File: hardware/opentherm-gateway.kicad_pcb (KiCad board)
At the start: 4 copper layers, 56 x 42 mm, 83 parts, among them J1 BOILER, J2 THERM, J3 USB-C, J5 5V IN, J6 NTC, Q1 MMBT2907A, Q2 MMBT2907A, Q3 MMBT2907A, Q4 MMBT2907A, Q5 MMBT2222A, Q6 MMBT2222A, SW1 RESET, SW2 BOOT, U1 MT3540-F23, U2 LTV-817S, U3 LTV-817S, U4 ESP32-C3-WROOM-02-N4, U5 AP2112K-3.3, U6 USBLC6-2SC6

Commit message: hardware: complete BOM with LCSC part numbers (JLCPCB format too), fix ESP32 module code, R17 330R for the green LED
Co-Authored-By: Claude Sonnet 5.5 <noreply@anthropic.com>
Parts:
- R17: value 1k -> 330
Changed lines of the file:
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@@
 			)
 		)
-		(property "Value" "1k"
+		(property "Value" "330"
 			(at 0 -1.65 180)
 			(layer "B.Fab")

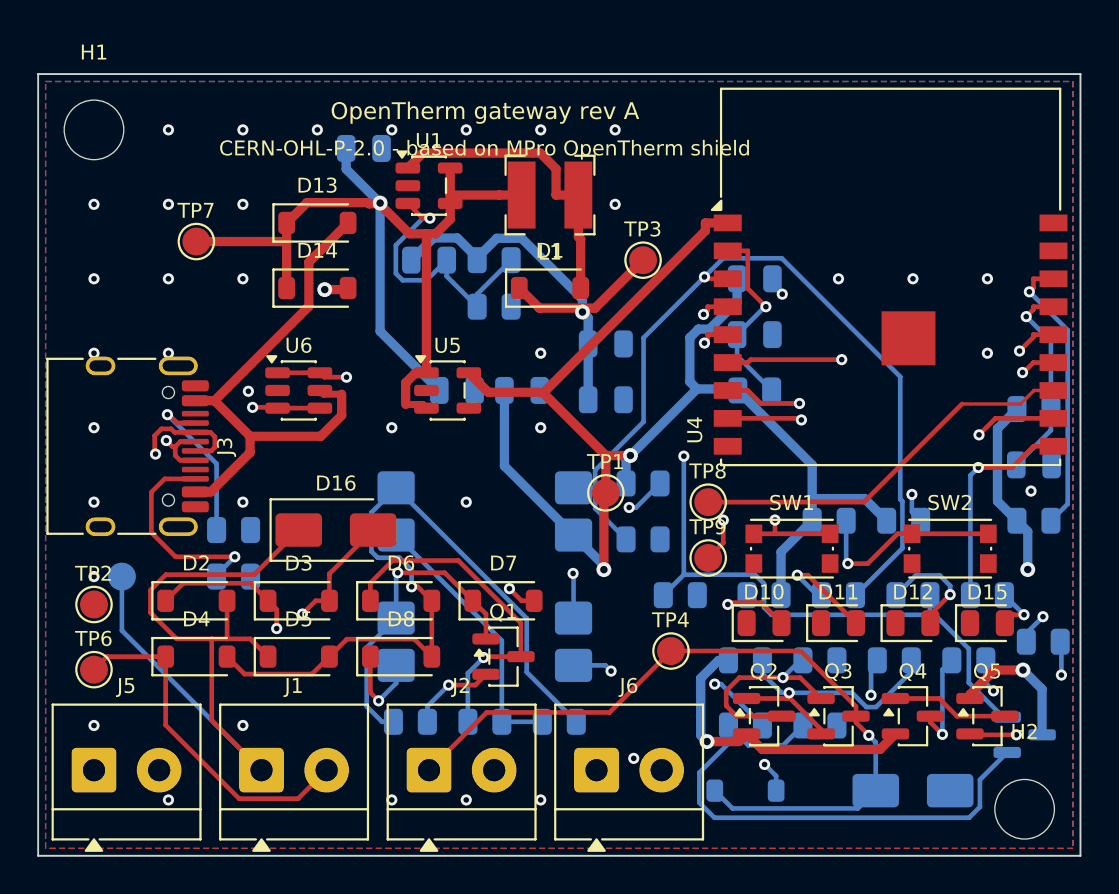
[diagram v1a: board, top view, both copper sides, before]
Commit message: hardware: plated hole in the ESP32 module GND pad for soldering from the bottom side
Co-Authored-By: Claude Sonnet 5.5 <noreply@anthropic.com>
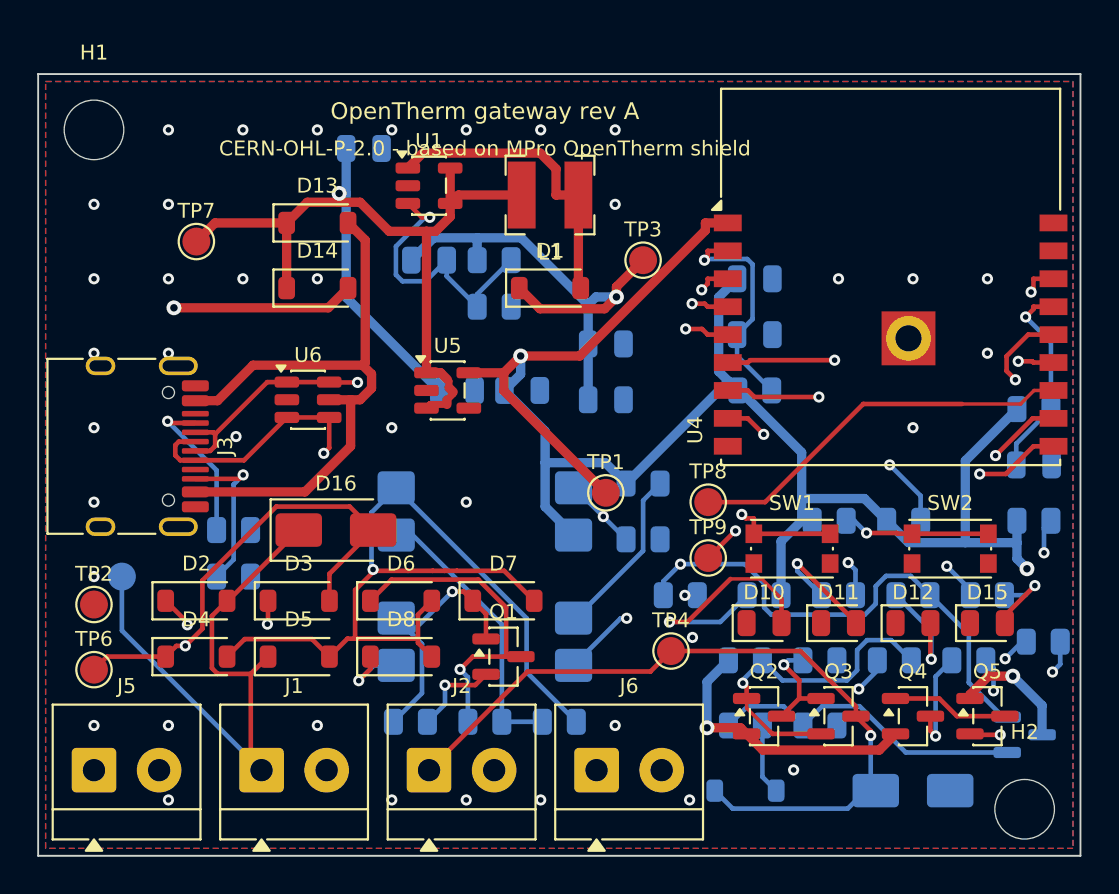
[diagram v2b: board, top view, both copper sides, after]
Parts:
- moved U6 0.71 mm to (14.5, 17.5)
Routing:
- net +3V3: track 124.4 -> 107.1 mm, vias 4 -> 3
- net Q6B: track 28.9 -> 17.3 mm
- net USB_DM: track 60.5 -> 49.6 mm, vias 3 -> 2
- net B1: track 41.5 -> 31.8 mm
- net SLAVE_IN: track 46.1 -> 36.7 mm, vias 1 -> 3
- net +24V: track 78.9 -> 69.5 mm
- net N_LED_PWR: track 4.62 -> 13.5 mm
- net N_D9A: track 10.6 -> 3.81 mm, vias 2 -> 0
- net Q2C: track 11.3 -> 5.80 mm
- net EN: track 26.9 -> 32.4 mm
- net BOOT: track 23.3 -> 17.9 mm
- net VBUS: track 28.7 -> 33.7 mm
- net 5V_IN: track 32.2 -> 36.4 mm
- net MASTER_IN: track 39.5 -> 42.7 mm
- net N_D7K: track 16.6 -> 13.6 mm
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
